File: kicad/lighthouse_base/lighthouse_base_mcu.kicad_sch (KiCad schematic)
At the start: 41 parts, among them J10 Conn_01x07, J3 Conn_01x07, J9 Conn_01x04, U5 STM32L412RBTx, U6 AT25SF081-SSHD-X, U7 RV-3028-C7, Y1 9HT11-32.768KDZB-T

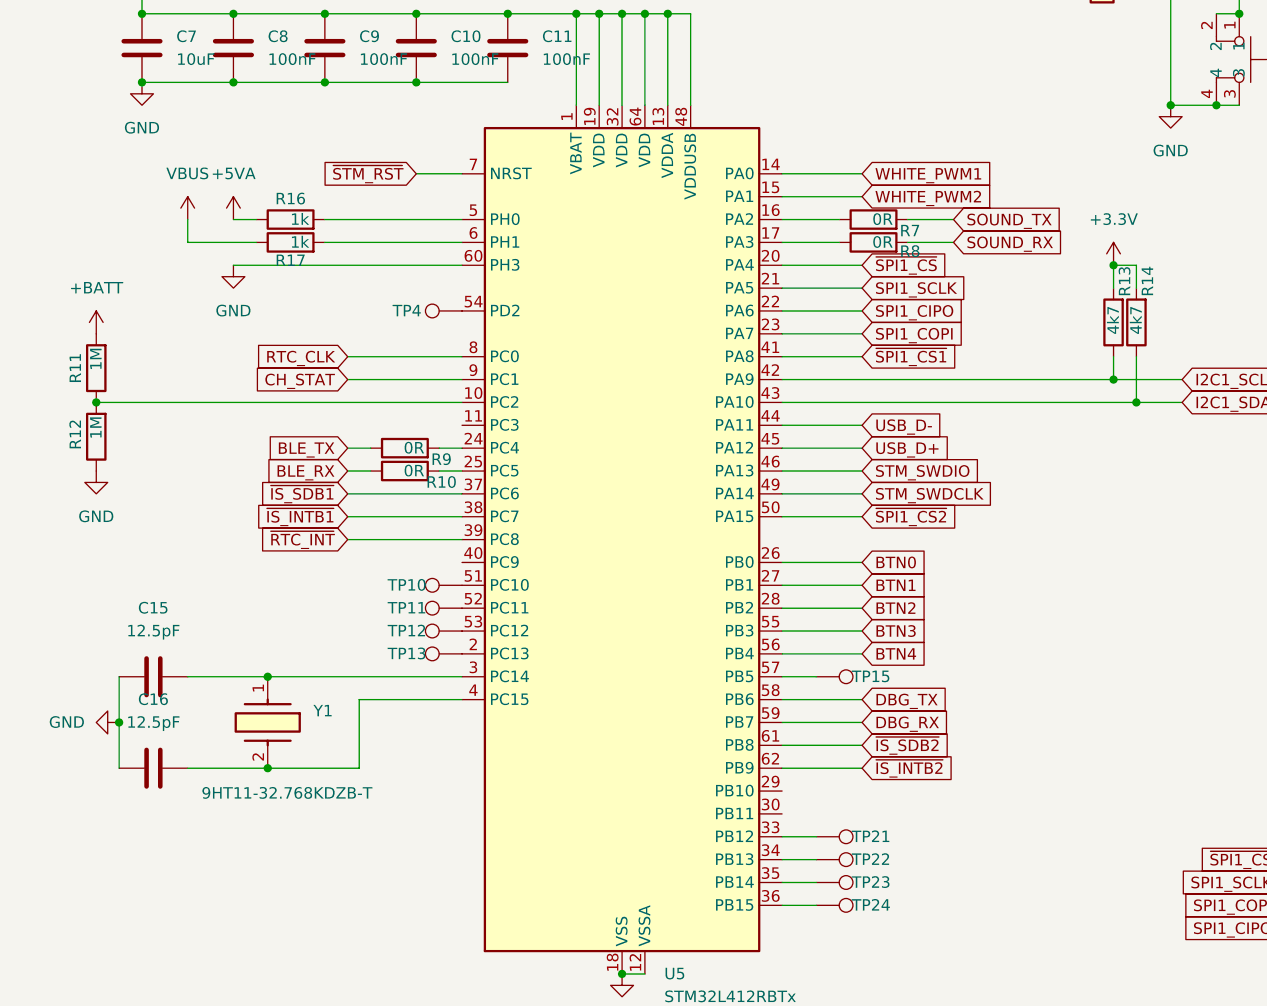
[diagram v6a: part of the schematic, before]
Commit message: ordererd lighthouse display
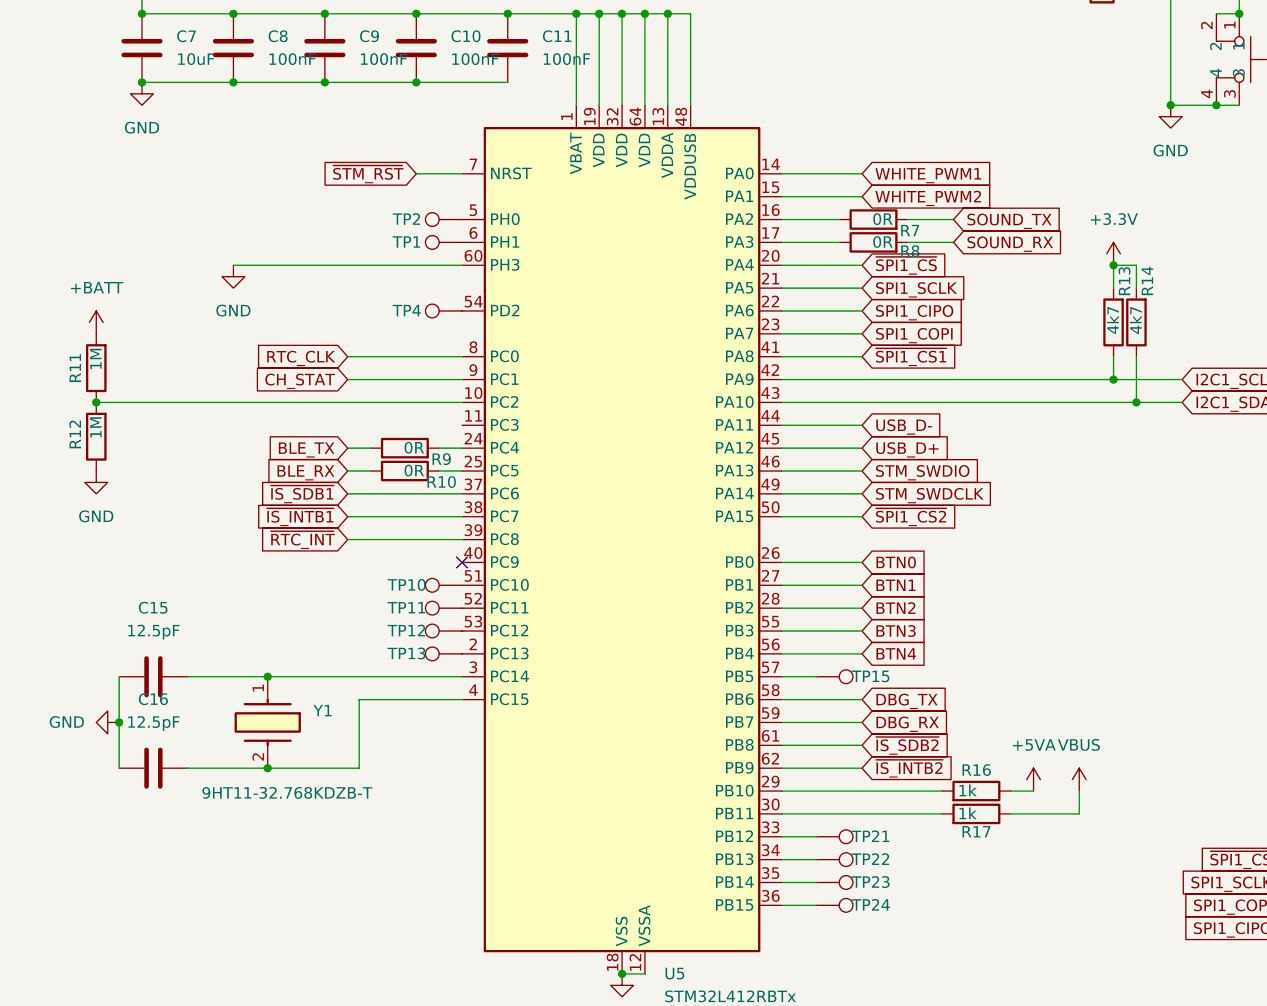
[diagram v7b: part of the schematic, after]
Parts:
- added TP1, TP2: TestPoint, TestPoint:TestPoint_Pad_D1.0mm, symbol Connector:TestPoint
- C12, C13, J10, J3, J9, R10, R7, R8, R9, TP10, TP11, TP12, TP13, TP15, TP21, TP22, TP23, TP24, TP4, U6: now left out of the parts list
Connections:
- net at R16.2: now also U5.29 (PB10); no longer U5.5 (PH0)
- net at R17.2: now also U5.30 (PB11); no longer U5.6 (PH1)
- new net: TP2.1, U5.5 (PH0)
- new net: TP1.1, U5.6 (PH1)
- no-connect marks 1 -> 2
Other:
- moved on the sheet: R16, R17
